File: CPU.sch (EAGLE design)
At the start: 10 parts, among them IC1 Z80CPU

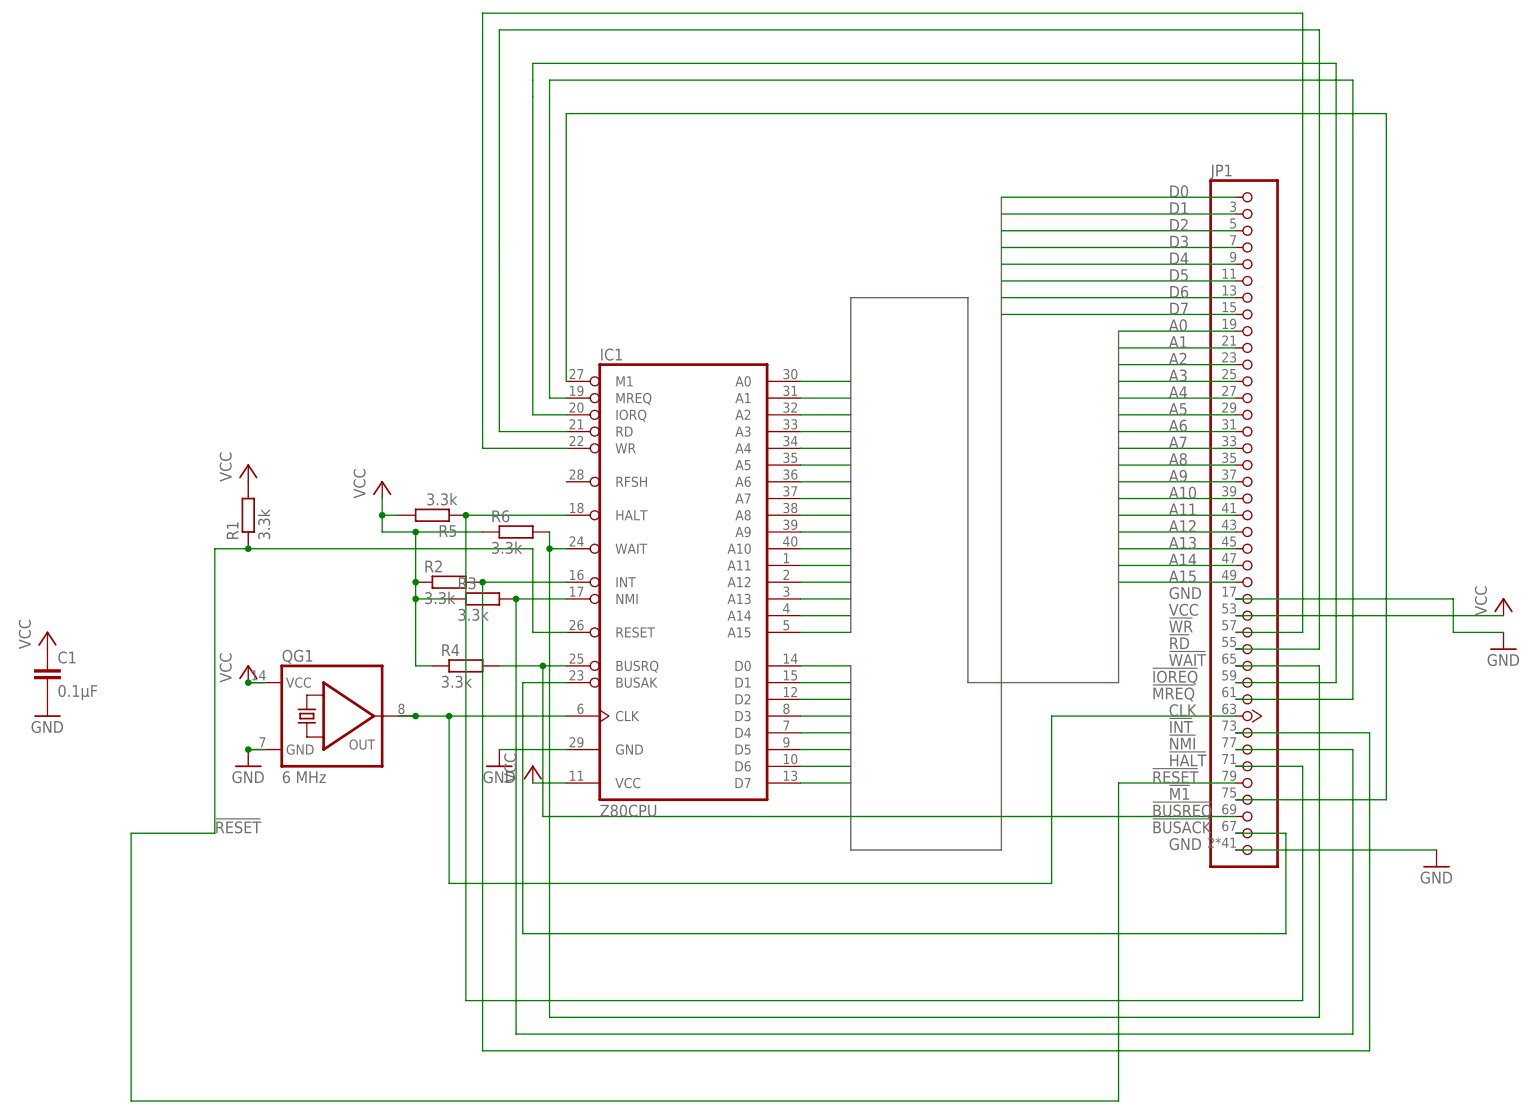
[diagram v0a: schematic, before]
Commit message: Restructure CPU Schematic
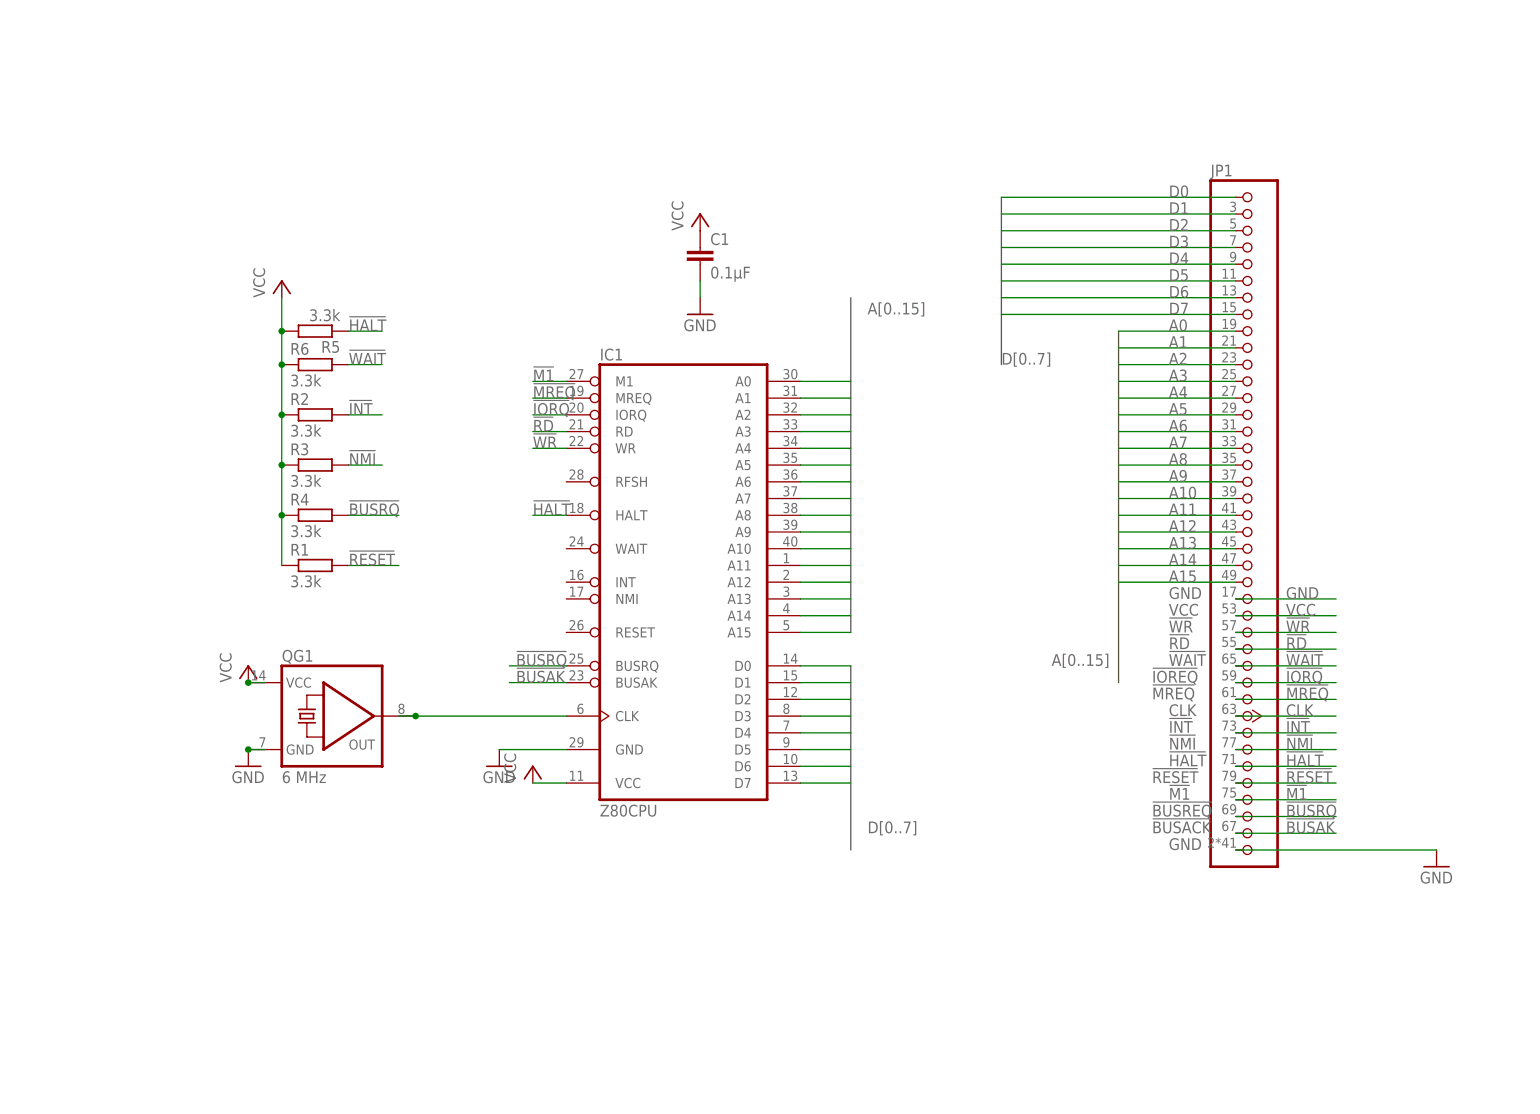
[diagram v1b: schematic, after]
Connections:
- net CLOCK renamed CLK
- net N$1 renamed !M1
- net N$10 renamed !WR
- net N$14 renamed !RD
- net N$16 renamed !IORQ
- net N$2 renamed !BUSRQ
- net N$22 renamed !BUSAK
- net N$8 renamed !MREQ
- net N$9 renamed !HALT
- removed net N$3: IC1.NMI, JP1.!NMI, R3.2
- removed net N$4: IC1.INT, JP1.!INT, R2.2
- removed net WAIT: IC1.WAIT, JP1.!WAIT, R6.2
- new net !INT: JP1.!INT, R2.2
- new net !NMI: JP1.!NMI, R3.2
- new net !WAIT: JP1.!WAIT, R6.2
- net !RESET: now also R1.2; no longer IC1.RESET, R1.1
- net VCC: now also R1.1; no longer R1.2
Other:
- moved on the sheet: C1, R1, R2, R3, R4, R5, R6

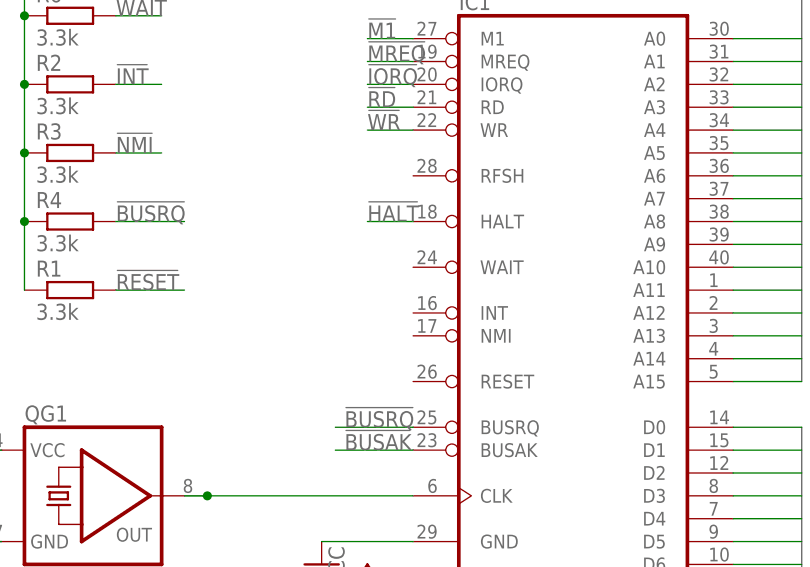
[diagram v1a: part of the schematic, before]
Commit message: Add missing wires
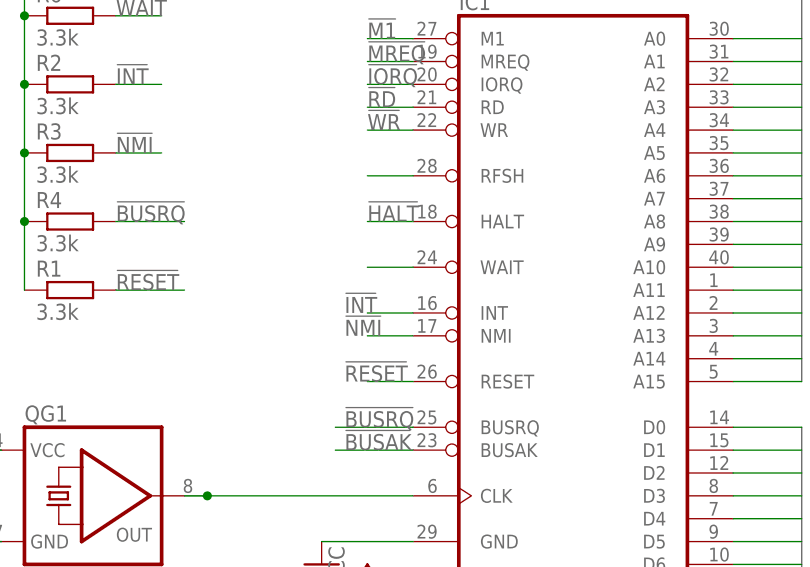
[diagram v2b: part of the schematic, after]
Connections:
- new net !RFSH: IC1.RFSH
- net !INT: now also IC1.INT
- net !NMI: now also IC1.NMI
- net !RESET: now also IC1.RESET
- net !WAIT: now also IC1.WAIT
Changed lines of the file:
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@@
 <?xml version="1.0" encoding="utf-8"?>
 <!DOCTYPE eagle SYSTEM "eagle.dtd">
-<eagle version="8.0.0">
+<eagle version="8.2.2">
 <drawing>
 <settings>
@@
 <label x="-38.1" y="60.96" size="1.778" layer="95"/>
 </segment>
+<segment>
+<pinref part="IC1" gate="1" pin="RESET"/>
+<wire x1="-5.08" y1="50.8" x2="-10.16" y2="50.8" width="0.1524" layer="91"/>
+<label x="-12.7" y="50.8" size="1.778" layer="95"/>
+</segment>
 </net>
 <net name="!WAIT" class="0">
@@
 <label x="-38.1" y="91.44" size="1.778" layer="95"/>
 </segment>
+<segment>
+<pinref part="IC1" gate="1" pin="WAIT"/>
+<wire x1="-5.08" y1="63.5" x2="-10.16" y2="63.5" width="0.1524" layer="91"/>
+</segment>
 </net>
 <net name="!MREQ" class="0">
@@
 <label x="-38.1" y="76.2" size="1.778" layer="95"/>
 </segment>
+<segment>
+<pinref part="IC1" gate="1" pin="NMI"/>
+<wire x1="-5.08" y1="55.88" x2="-10.16" y2="55.88" width="0.1524" layer="91"/>
+<label x="-12.7" y="55.88" size="1.778" layer="95"/>
+</segment>
 </net>
 <net name="!INT" class="0">
@@
 <wire x1="-38.1" y1="83.82" x2="-33.02" y2="83.82" width="0.1524" layer="91"/>
 <label x="-38.1" y="83.82" size="1.778" layer="95"/>
+</segment>
+<segment>
+<pinref part="IC1" gate="1" pin="INT"/>
+<wire x1="-5.08" y1="58.42" x2="-10.16" y2="58.42" width="0.1524" layer="91"/>
+<label x="-12.7" y="58.42" size="1.778" layer="95"/>
 </segment>
 </net>
@@
 </segment>
 </net>
+<net name="!RFSH" class="0">
+<segment>
+<pinref part="IC1" gate="1" pin="RFSH"/>
+<wire x1="-5.08" y1="73.66" x2="-10.16" y2="73.66" width="0.1524" layer="91"/>
+</segment>
+</net>
